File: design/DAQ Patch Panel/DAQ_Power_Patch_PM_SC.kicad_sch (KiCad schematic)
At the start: 12 parts, among them J2 GND, J4 Voltage Input Terminal, J7 Sensor 1 Terminal, J8 Sensor 1 Output

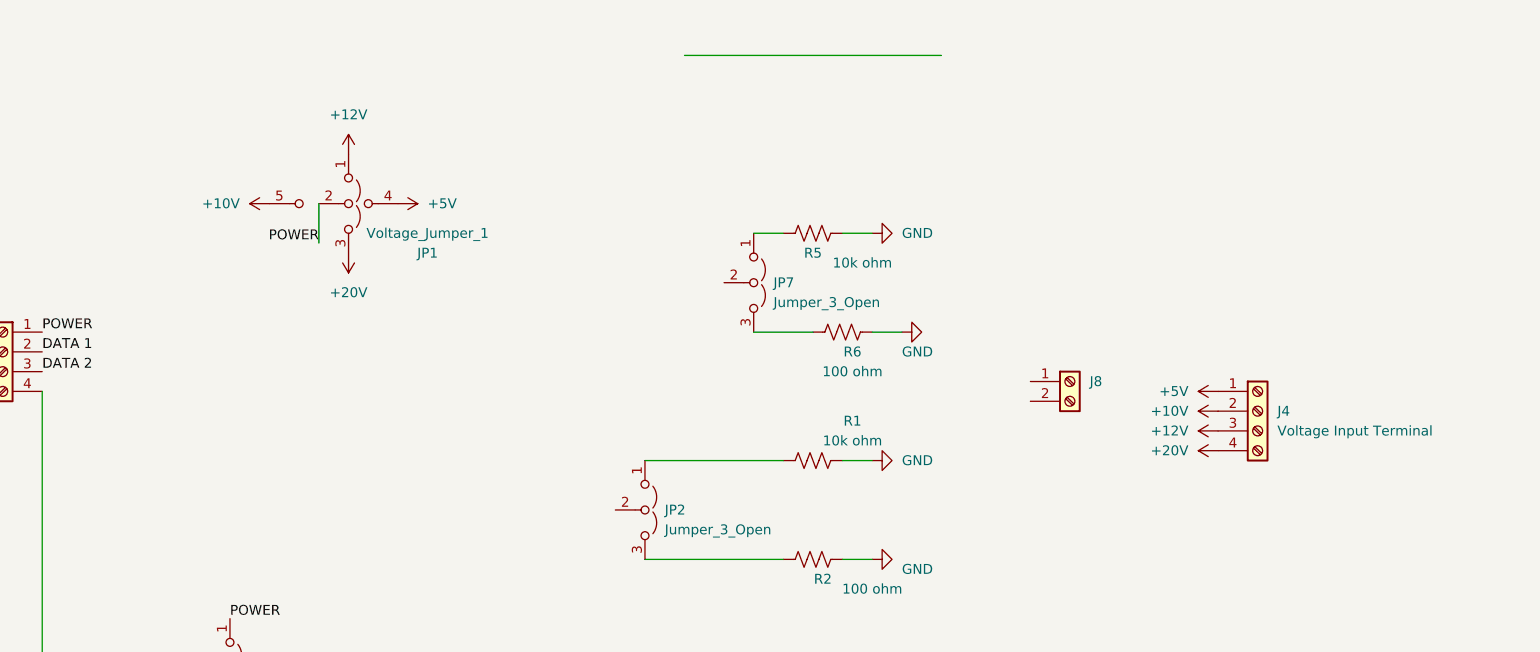
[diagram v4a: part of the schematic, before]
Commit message: Added RC-Low Pass filter
Added RC-Low Pass filter to data lines
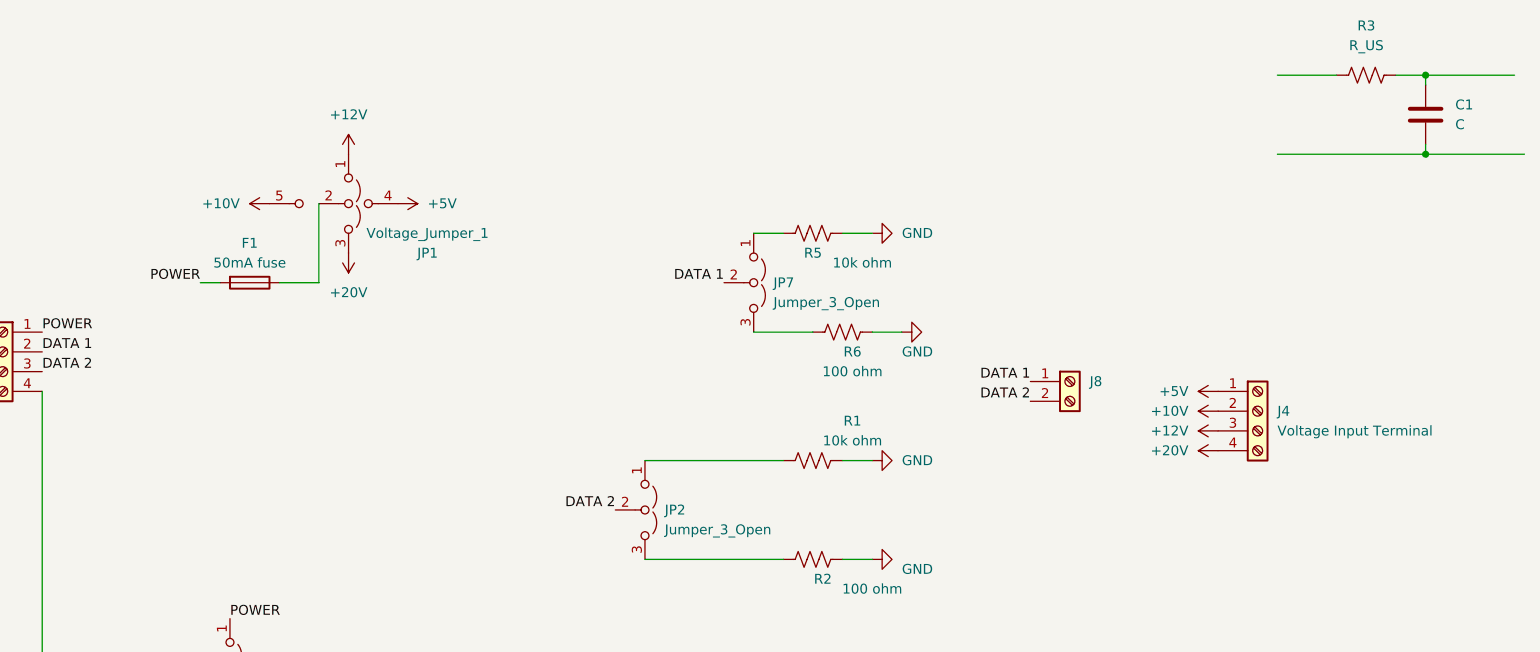
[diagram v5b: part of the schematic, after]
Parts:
- added C1: C, symbol Device:C
- added F1: 50mA fuse, symbol Device:Fuse
- added R3: R_US, symbol Device:R_US
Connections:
- net DATA 1: now also J8.1 (Pin_1), JP7.2 (C)
- net DATA 2: now also J8.2 (Pin_2), JP2.2 (C)
- net POWER: now also F1.2; no longer JP1.2 (C)
- new net: C1.1, R3.2
- new net: F1.1, JP1.2 (C)
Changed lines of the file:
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@@
     (company "Waterloo Rocketry ")
   )
+  (junction (at 250.19 67.31) (diameter 0) (color 0 0 0 0)
+  )
+  (junction (at 250.19 57.15) (diameter 0) (color 0 0 0 0)
+  )
   (wire (pts (xy 149.86 119.38) (xy 167.64 119.38))
     (stroke (width 0) (type default))
   )
+  (wire (pts (xy 250.19 57.15) (xy 261.62 57.15))
+    (stroke (width 0) (type default))
+  )
   (wire (pts (xy 163.83 90.17) (xy 171.45 90.17))
     (stroke (width 0) (type default))
@@
     (stroke (width 0) (type default))
   )
+  (wire (pts (xy 95.25 83.82) (xy 92.71 83.82))
+    (stroke (width 0) (type default))
+  )
   (wire (pts (xy 175.26 77.47) (xy 179.07 77.47))
     (stroke (width 0) (type default))
   )
+  (wire (pts (xy 231.14 57.15) (xy 238.76 57.15))
+    (stroke (width 0) (type default))
+  )
   (wire (pts (xy 163.83 77.47) (xy 167.64 77.47))
     (stroke (width 0) (type default))
@@
     (stroke (width 0) (type default))
   )
+  (wire (pts (xy 102.87 83.82) (xy 107.95 83.82))
+    (stroke (width 0) (type default))
+  )
   (wire (pts (xy 179.07 119.38) (xy 175.26 119.38))
     (stroke (width 0) (type default))
@@
     (stroke (width 0) (type default))
   )
-  (wire (pts (xy 154.94 54.61) (xy 187.96 54.61))
+  (wire (pts (xy 250.19 67.31) (xy 262.89 67.31))
+    (stroke (width 0) (type default))
+  )
+  (wire (pts (xy 250.19 57.15) (xy 250.19 58.42))
     (stroke (width 0) (type default))
   )
@@
     (stroke (width 0) (type default))
   )
+  (wire (pts (xy 246.38 57.15) (xy 250.19 57.15))
+    (stroke (width 0) (type default))
+  )
+  (wire (pts (xy 250.19 66.04) (xy 250.19 67.31))
+    (stroke (width 0) (type default))
+  )
   (wire (pts (xy 72.39 97.79) (xy 72.39 133.35))
     (stroke (width 0) (type default))
   )
-  (wire (pts (xy 107.95 73.66) (xy 107.95 78.74))
+  (wire (pts (xy 107.95 73.66) (xy 107.95 83.82))
+    (stroke (width 0) (type default))
+  )
+  (wire (pts (xy 231.14 67.31) (xy 250.19 67.31))
     (stroke (width 0) (type default))
   )
@@
     (effects (font (size 1.27 1.27)) (justify left bottom))
   )
-  (label "POWER" (at 107.95 78.74 180) (fields_autoplaced)
+  (label "DATA 2" (at 199.39 99.06 180) (fields_autoplaced)
+    (effects (font (size 1.27 1.27)) (justify right bottom))
+  )
+  (label "POWER" (at 92.71 83.82 180) (fields_autoplaced)
+    (effects (font (size 1.27 1.27)) (justify right bottom))
+  )
+  (label "DATA 1" (at 199.39 96.52 180) (fields_autoplaced)
+    (effects (font (size 1.27 1.27)) (justify right bottom))
+  )
+  (label "DATA 2" (at 146.05 113.03 180) (fields_autoplaced)
     (effects (font (size 1.27 1.27)) (justify right bottom))
   )
@@
     (effects (font (size 1.27 1.27)) (justify left bottom))
   )
+  (label "DATA 1" (at 160.02 83.82 180) (fields_autoplaced)
+    (effects (font (size 1.27 1.27)) (justify right bottom))
+  )
   (label "POWER" (at 96.52 127 0) (fields_autoplaced)
     (effects (font (size 1.27 1.27)) (justify left bottom))
@@
     )
   )
+  (symbol (lib_id "Device:C") (at 250.19 62.23 0) (unit 1)
+    (in_bom yes) (on_board yes) (dnp no) (fields_autoplaced)
+    (property "Reference" "C1" (at 254 60.96 0)
+      (effects (font (size 1.27 1.27)) (justify left))
+    )
+    (property "Value" "C" (at 254 63.5 0)
+      (effects (font (size 1.27 1.27)) (justify left))
+    )
+    (property "Footprint" "" (at 251.1552 66.04 0)
+      (effects (font (size 1.27 1.27)) hide)
+    )
+    (property "Datasheet" "~" (at 250.19 62.23 0)
+      (effects (font (size 1.27 1.27)) hide)
+    )
+    (pin "1")
+    (pin "2")
+    (instances
+      (project "DAQ_Power_Patch_PM_SC"
+        (path "/da75d2ac-4c40-407d-8f74-3497a5ffc88d"
+          (reference "C1") (unit 1)
+        )
+      )
+    )
+  )
   (symbol (lib_name "+10V_1") (lib_id "power:+10V") (at 111.76 80.01 180) (unit 1)
     (in_bom yes) (on_board yes) (dnp no) (fields_autoplaced)
@@
         (path "/da75d2ac-4c40-407d-8f74-3497a5ffc88d"
           (reference "R1") (unit 1)
+        )
+      )
+    )
+  )
+  (symbol (lib_id "Device:Fuse") (at 99.06 83.82 270) (unit 1)
+    (in_bom yes) (on_board yes) (dnp no) (fields_autoplaced)
+    (property "Reference" "F1" (at 99.06 78.74 90)
+      (effects (font (size 1.27 1.27)))
+    )
+    (property "Value" "50mA fuse" (at 99.06 81.28 90)
+      (effects (font (size 1.27 1.27)))
+    )
+    (property "Footprint" "" (at 99.06 82.042 90)
+      (effects (font (size 1.27 1.27)) hide)
+    )
+    (property "Datasheet" "~" (at 99.06 83.82 0)
+      (effects (font (size 1.27 1.27)) hide)
+    )
+    (pin "1")
+    (pin "2")
+    (instances
+      (project "DAQ_Power_Patch_PM_SC"
+        (path "/da75d2ac-4c40-407d-8f74-3497a5ffc88d"
+          (reference "F1") (unit 1)
         )
       )
@@
         )
       )
+    )
+  )
+  (symbol (lib_id "Device:R_US") (at 242.57 57.15 90) (unit 1)
+    (in_bom yes) (on_board yes) (dnp no) (fields_autoplaced)
+    (property "Reference" "R3" (at 242.57 50.8 90)
+      (effects (font (size 1.27 1.27)))
+    )
+    (property "Value" "R_US" (at 242.57 53.34 90)
+      (effects (font (size 1.27 1.27)))
+    )
+    (property "Footprint" "" (at 242.824 56.134 90)
+      (effects (font (size 1.27 1.27)) hide)
+    )
+    (property "Datasheet" "~" (at 242.57 57.15 0)
+      (effects (font (size 1.27 1.27)) hide)
+    )
+    (pin "1")
+    (pin "2")
+    (instances
+      (project "DAQ_Power_Patch_PM_SC"
+        (path "/da75d2ac-4c40-407d-8f74-3497a5ffc88d"
+          (reference "R3") (unit 1)
+        )
+      )

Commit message: Changes
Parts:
- added C2: 80nF, symbol Device:C
- added R4: 100 ohms, symbol Device:R_US
- C1: value C -> 80nF
- R3: value R_US -> 100 ohms
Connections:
- net DATA 1: now also C2.1, R4.1, R4.2
- net DATA 2: now also C1.1, R3.1, R3.2
- net GND: now also C1.2, C2.2
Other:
- moved on the sheet: C1, F1, JP1, JP2, R1, R2, R3

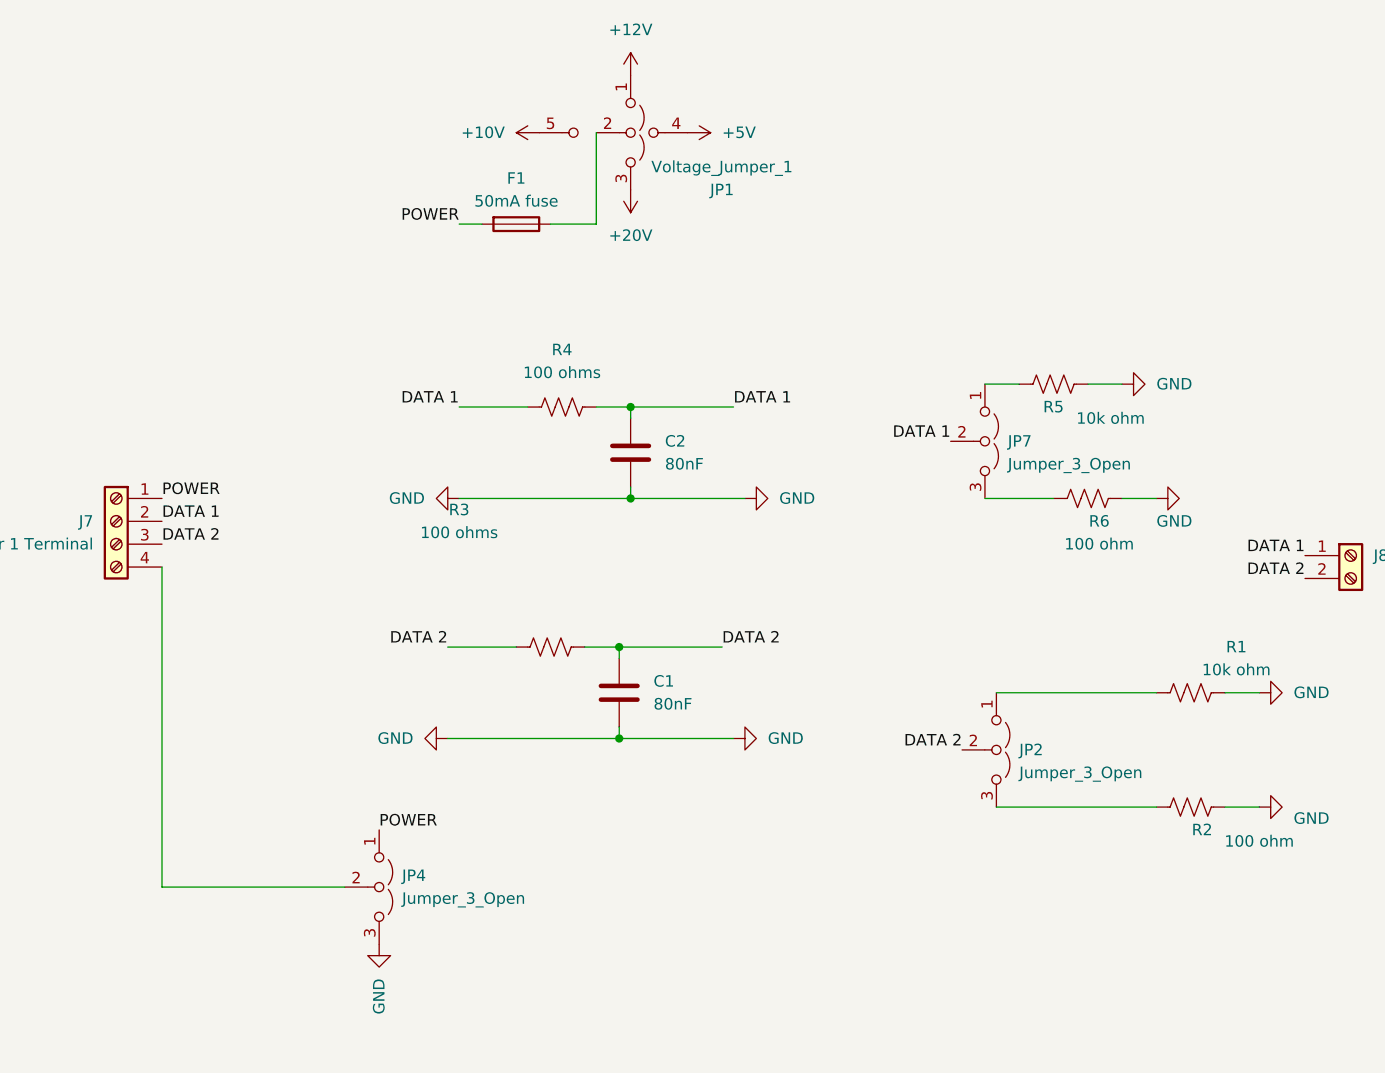
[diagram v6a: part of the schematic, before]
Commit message: Jack Edits and Aesthetic Stuff
Made sure the nets for the RC filter input are not connected to the output.
Renamed the jumpers to something meaningful
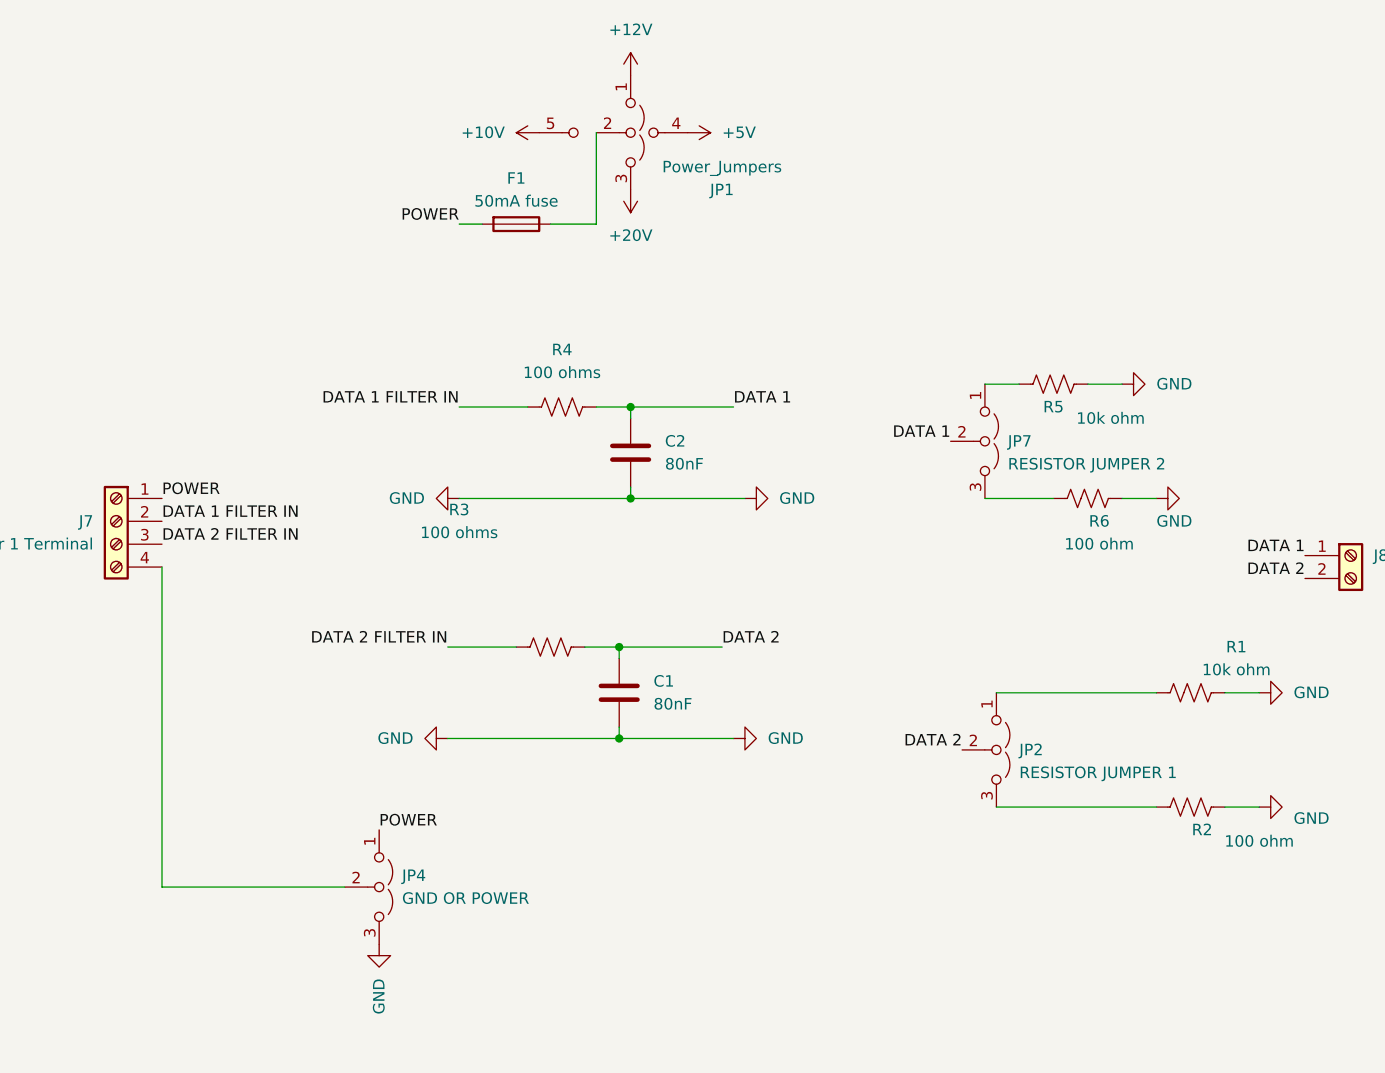
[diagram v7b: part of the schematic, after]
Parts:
- JP1: value Voltage_Jumper_1 -> Power_Jumpers
- JP2: value Jumper_3_Open -> RESISTOR JUMPER 1
- JP4: value Jumper_3_Open -> GND OR POWER
- JP7: value Jumper_3_Open -> RESISTOR JUMPER 2
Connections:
- net DATA 1: no longer J7.2 (Pin_2), R4.1
- net DATA 2: no longer J7.3 (Pin_3), R3.1
- new net DATA 1 FILTER IN: J7.2 (Pin_2), R4.1
- new net DATA 2 FILTER IN: J7.3 (Pin_3), R3.1
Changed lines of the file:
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@@
   (title_block
     (title "DAQ_PATCH_PANEL")
-    (date "2023-11-04")
-    (rev "V-4")
+    (date "2023-11-13")
+    (rev "V-5")
     (company "Waterloo Rocketry ")
   )
@@
     (effects (font (size 1.27 1.27)) (justify right bottom))
   )
-  (label "DATA 1" (at 105.41 80.01 180) (fields_autoplaced)
+  (label "DATA 1 FILTER IN" (at 105.41 80.01 180) (fields_autoplaced)
     (effects (font (size 1.27 1.27)) (justify right bottom))
   )
@@
     (effects (font (size 1.27 1.27)) (justify left bottom))
   )
-  (label "DATA 2" (at 72.39 95.25 0) (fields_autoplaced)
+  (label "DATA 2 FILTER IN" (at 72.39 95.25 0) (fields_autoplaced)
     (effects (font (size 1.27 1.27)) (justify left bottom))
   )
@@
     (effects (font (size 1.27 1.27)) (justify right bottom))
   )
-  (label "DATA 2" (at 104.14 106.68 180) (fields_autoplaced)
+  (label "DATA 2 FILTER IN" (at 104.14 106.68 180) (fields_autoplaced)
     (effects (font (size 1.27 1.27)) (justify right bottom))
   )
@@
     (effects (font (size 1.27 1.27)) (justify left bottom))
   )
-  (label "DATA 1" (at 72.39 92.71 0) (fields_autoplaced)
+  (label "DATA 1 FILTER IN" (at 72.39 92.71 0) (fields_autoplaced)
     (effects (font (size 1.27 1.27)) (justify left bottom))
   )
@@
       (effects (font (size 1.27 1.27)))
     )
-    (property "Value" "Voltage_Jumper_1" (at 134.62 53.34 90)
+    (property "Value" "Power_Jumpers" (at 134.62 53.34 90)
       (effects (font (size 1.27 1.27)))
     )
@@
       (effects (font (size 1.27 1.27)) (justify left))
     )
-    (property "Value" "Jumper_3_Open" (at 167.64 120.65 90)
+    (property "Value" "RESISTOR JUMPER 1" (at 167.64 120.65 90)
       (effects (font (size 1.27 1.27)) (justify left))
     )
@@
       (effects (font (size 1.27 1.27)) (justify left))
     )
-    (property "Value" "Jumper_3_Open" (at 99.06 134.62 90)
+    (property "Value" "GND OR POWER" (at 99.06 134.62 90)
       (effects (font (size 1.27 1.27)) (justify left))
     )
@@
       (effects (font (size 1.27 1.27)) (justify left))
     )
-    (property "Value" "Jumper_3_Open" (at 166.37 86.36 90)
-      (effects (font (size 1.27 1.27)) (justify left))
-    )
+    (property "Value" "RESISTOR JUMPER 2" (at 166.37 86.36 90)
+      (effects (font (size 1.27 1.27)) (justify left))
+    )
